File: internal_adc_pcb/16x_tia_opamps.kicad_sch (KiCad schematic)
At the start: 46 parts, among them U14 TLV9064, U15 TLV9064, U16 TLV9064, U17 TLV9064

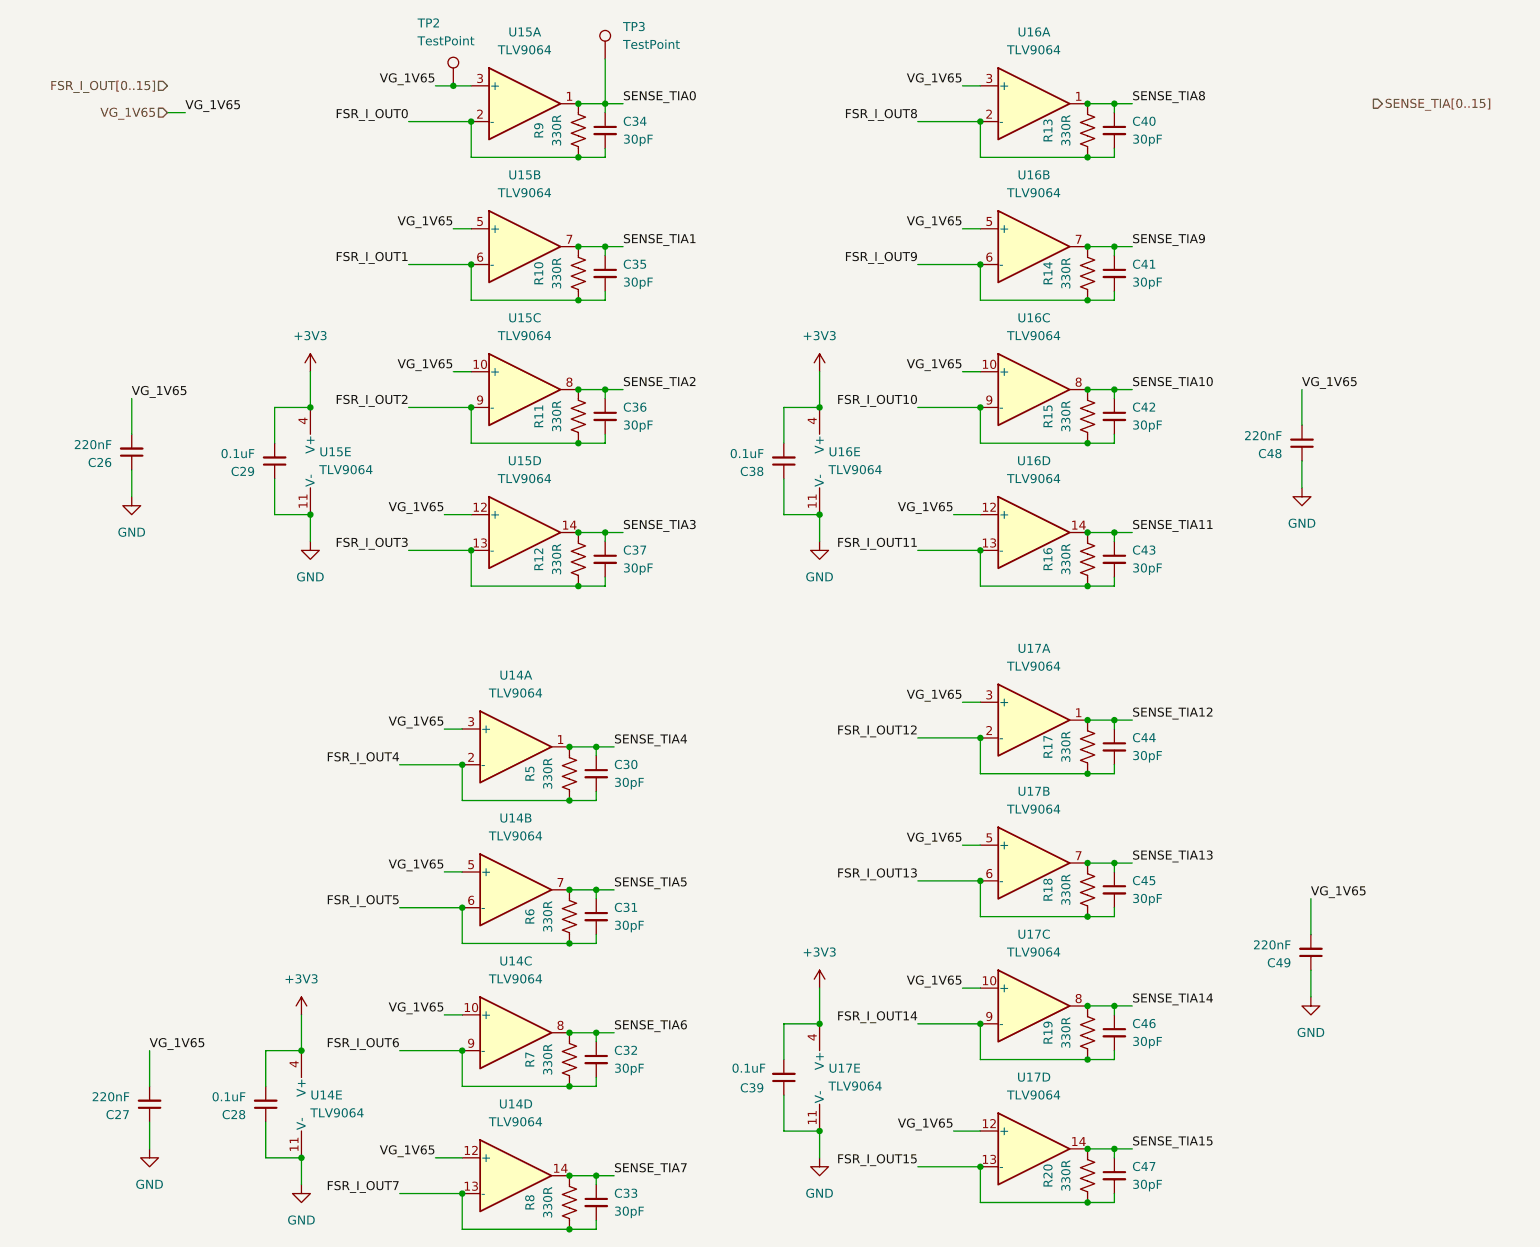
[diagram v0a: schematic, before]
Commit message: adjust VG issue for internal ADC version; changed naming for VG
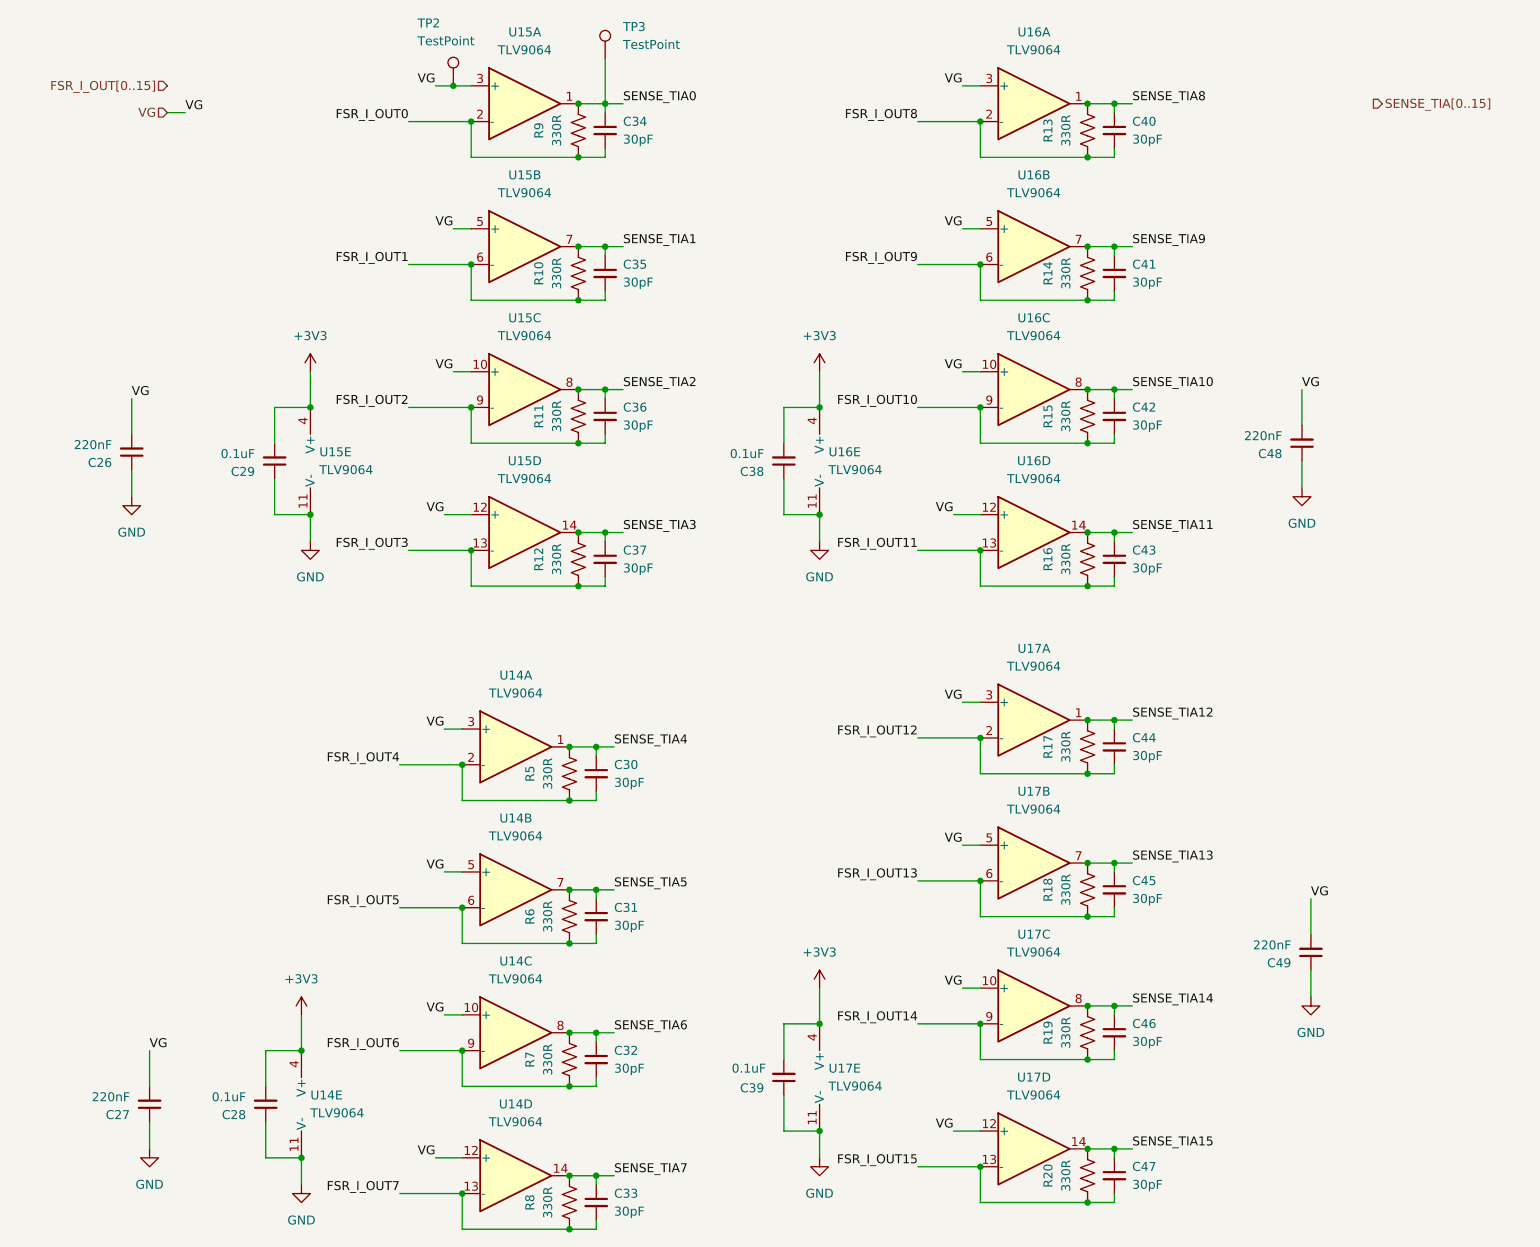
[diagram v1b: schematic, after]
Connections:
- net VG_1V65 renamed VG
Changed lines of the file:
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@@
 		)
 	)
-	(label "VG_1V65"
+	(label "VG"
 		(at 38.1 33.02 0)
 		(effects
@@
 		)
 	)
-	(label "VG_1V65"
+	(label "VG"
 		(at 76.2 69.85 180)
 		(effects
@@
 		)
 	)
-	(label "VG_1V65"
+	(label "VG"
 		(at 148.59 29.21 180)
 		(effects
@@
 		)
 	)
-	(label "VG_1V65"
+	(label "VG"
 		(at 148.59 49.53 180)
 		(effects
@@
 		)
 	)
-	(label "VG_1V65"
+	(label "VG"
 		(at 76.2 49.53 180)
 		(effects
@@
 		)
 	)
-	(label "VG_1V65"
+	(label "VG"
 		(at 147.32 90.17 180)
 		(effects
@@
 		)
 	)
-	(label "VG_1V65"
+	(label "VG"
 		(at 74.93 90.17 180)
 		(effects
@@
 		)
 	)
-	(label "VG_1V65"
+	(label "VG"
 		(at 147.32 177.8 180)
 		(effects
@@
 		)
 	)
-	(label "VG_1V65"
+	(label "VG"
 		(at 148.59 116.84 180)
 		(effects
@@
 		)
 	)
-	(label "VG_1V65"
+	(label "VG"
 		(at 74.93 120.65 180)
 		(effects
@@
 		)
 	)
-	(label "VG_1V65"
+	(label "VG"
 		(at 73.66 181.61 180)
 		(effects
@@
 		)
 	)
-	(label "VG_1V65"
+	(label "VG"
 		(at 196.85 72.39 0)
 		(effects
@@
 		)
 	)
-	(label "VG_1V65"
+	(label "VG"
 		(at 74.93 140.97 180)
 		(effects
@@
 		)
 	)
-	(label "VG_1V65"
+	(label "VG"
 		(at 30.48 73.66 0)
 		(effects
@@
 		)
 	)
-	(label "VG_1V65"
+	(label "VG"
 		(at 198.12 144.78 0)
 		(effects
@@
 		)
 	)
-	(label "VG_1V65"
+	(label "VG"
 		(at 148.59 137.16 180)
 		(effects
@@
 		)
 	)
-	(label "VG_1V65"
+	(label "VG"
 		(at 148.59 157.48 180)
 		(effects
@@
 		)
 	)
-	(label "VG_1V65"
+	(label "VG"
 		(at 73.66 29.21 180)
 		(effects
@@
 		)
 	)
-	(label "VG_1V65"
+	(label "VG"
 		(at 74.93 161.29 180)
 		(effects
@@
 		)
 	)
-	(label "VG_1V65"
+	(label "VG"
 		(at 148.59 69.85 180)
 		(effects
@@
 		)
 	)
-	(label "VG_1V65"
+	(label "VG"
 		(at 33.02 166.37 0)
 		(effects
@@
 		)
 	)
-	(hierarchical_label "VG_1V65"
+	(hierarchical_label "VG"
 		(shape input)
 		(at 35.56 33.02 180)

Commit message: update pcb for internal adc version
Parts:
- C26, C27, C28, C29, C30, C31, C32, C33, C34, C35, C36, C37, C38, C39, C40, C41, C42, C43, C44, C45, C46, C47, C48, C49, R10, R11, R12, R13, R14, R15, R16, R17, R18, R19, R20, R5, R6, R7, R8, R9: footprint (none) -> Capacitor_SMD:C_0603_1608Metric
- TP2, TP3: footprint (none) -> TestPoint:TestPoint_Keystone_5000-5004_Miniature
- U14, U15, U16, U17: footprint (none) -> Package_SO:TSSOP-14_4.4x5mm_P0.65mm
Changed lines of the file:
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@@
 			)
 		)
-		(property "Footprint" ""
+		(property "Footprint" "Capacitor_SMD:C_0603_1608Metric"
 			(at 30.48 81.28 0)
 			(hide yes)
@@
 			)
 		)
-		(property "Footprint" ""
+		(property "Footprint" "TestPoint:TestPoint_Keystone_5000-5004_Miniature"
 			(at 81.28 29.21 0)
 			(hide yes)
@@
 			)
 		)
-		(property "Footprint" ""
+		(property "Footprint" "Capacitor_SMD:C_0603_1608Metric"
 			(at 97.79 55.88 0)
 			(hide yes)
@@
 			)
 		)
-		(property "Footprint" ""
+		(property "Footprint" "Capacitor_SMD:C_0603_1608Metric"
 			(at 50.8 82.55 0)
 			(hide yes)
@@
 			)
 		)
-		(property "Footprint" ""
+		(property "Footprint" "Package_SO:TSSOP-14_4.4x5mm_P0.65mm"
 			(at 129.54 167.64 0)
 			(hide yes)
@@
 			)
 		)
-		(property "Footprint" ""
+		(property "Footprint" "Capacitor_SMD:C_0603_1608Metric"
 			(at 167.386 76.454 90)
 			(hide yes)
@@
 			)
 		)
-		(property "Footprint" ""
+		(property "Footprint" "Capacitor_SMD:C_0603_1608Metric"
 			(at 93.726 127.254 90)
 			(hide yes)
@@
 			)
 		)
-		(property "Footprint" ""
+		(property "Footprint" "Capacitor_SMD:C_0603_1608Metric"
 			(at 170.18 143.51 0)
 			(hide yes)
@@
 			)
 		)
-		(property "Footprint" ""
+		(property "Footprint" "Capacitor_SMD:C_0603_1608Metric"
 			(at 96.52 187.96 0)
 			(hide yes)
@@
 			)
 		)
-		(property "Footprint" ""
+		(property "Footprint" "Capacitor_SMD:C_0603_1608Metric"
 			(at 33.02 173.99 0)
 			(hide yes)
@@
 			)
 		)
-		(property "Footprint" ""
+		(property "Footprint" "Capacitor_SMD:C_0603_1608Metric"
 			(at 170.18 35.56 0)
 			(hide yes)
@@
 			)
 		)
-		(property "Footprint" ""
+		(property "Footprint" "Package_SO:TSSOP-14_4.4x5mm_P0.65mm"
 			(at 83.82 161.29 0)
 			(hide yes)
@@
 			)
 		)
-		(property "Footprint" ""
+		(property "Footprint" "Capacitor_SMD:C_0603_1608Metric"
 			(at 170.18 55.88 0)
 			(hide yes)
@@
 			)
 		)
-		(property "Footprint" ""
+		(property "Footprint" "Capacitor_SMD:C_0603_1608Metric"
 			(at 167.386 184.404 90)
 			(hide yes)
@@
 			)
 		)
-		(property "Footprint" ""
+		(property "Footprint" "Package_SO:TSSOP-14_4.4x5mm_P0.65mm"
 			(at 157.48 90.17 0)
 			(hide yes)
@@
 			)
 		)
-		(property "Footprint" ""
+		(property "Footprint" "Capacitor_SMD:C_0603_1608Metric"
 			(at 198.12 152.4 0)
 			(hide yes)
@@
 			)
 		)
-		(property "Footprint" ""
+		(property "Footprint" "Capacitor_SMD:C_0603_1608Metric"
 			(at 96.52 127 0)
 			(hide yes)
@@
 			)
 		)
-		(property "Footprint" ""
+		(property "Footprint" "Capacitor_SMD:C_0603_1608Metric"
 			(at 97.79 35.56 0)
 			(hide yes)
@@
 			)
 		)
-		(property "Footprint" ""
+		(property "Footprint" "Capacitor_SMD:C_0603_1608Metric"
 			(at 167.386 143.764 90)
 			(hide yes)
@@
 			)
 		)
-		(property "Footprint" ""
+		(property "Footprint" "Capacitor_SMD:C_0603_1608Metric"
 			(at 167.386 164.084 90)
 			(hide yes)
@@
 			)
 		)
-		(property "Footprint" ""
+		(property "Footprint" "Capacitor_SMD:C_0603_1608Metric"
 			(at 167.386 123.444 90)
 			(hide yes)
@@
 			)
 		)
-		(property "Footprint" ""
+		(property "Footprint" "Capacitor_SMD:C_0603_1608Metric"
 			(at 94.996 56.134 90)
 			(hide yes)
@@
 			)
 		)
-		(property "Footprint" ""
+		(property "Footprint" "Package_SO:TSSOP-14_4.4x5mm_P0.65mm"
 			(at 85.09 29.21 0)
 			(hide yes)
@@
 			)
 		)
-		(property "Footprint" ""
+		(property "Footprint" "Capacitor_SMD:C_0603_1608Metric"
 			(at 94.996 35.814 90)
 			(hide yes)
@@
 			)
 		)
-		(property "Footprint" ""
+		(property "Footprint" "Capacitor_SMD:C_0603_1608Metric"
 			(at 123.19 82.55 0)
 			(hide yes)
@@
 			)
 		)
-		(property "Footprint" ""
+		(property "Footprint" "Capacitor_SMD:C_0603_1608Metric"
 			(at 167.386 56.134 90)
 			(hide yes)
@@
 			)
 		)
-		(property "Footprint" ""
+		(property "Footprint" "Capacitor_SMD:C_0603_1608Metric"
 			(at 123.19 170.18 0)
 			(hide yes)
@@
 			)
 		)
-		(property "Footprint" ""
+		(property "Footprint" "Package_SO:TSSOP-14_4.4x5mm_P0.65mm"
 			(at 157.48 157.48 0)
 			(hide yes)
@@
 			)
 		)
-		(property "Footprint" ""
+		(property "Footprint" "Capacitor_SMD:C_0603_1608Metric"
 			(at 97.79 96.52 0)
 			(hide yes)
@@
 			)
 		)
-		(property "Footprint" ""
+		(property "Footprint" "Capacitor_SMD:C_0603_1608Metric"
 			(at 96.52 147.32 0)
 			(hide yes)
@@
 			)
 		)
-		(property "Footprint" ""
+		(property "Footprint" "Package_SO:TSSOP-14_4.4x5mm_P0.65mm"
 			(at 55.88 171.45 0)
 			(hide yes)
@@
 			)
 		)
-		(property "Footprint" ""
+		(property "Footprint" "Package_SO:TSSOP-14_4.4x5mm_P0.65mm"
 			(at 57.15 80.01 0)
 			(hide yes)
@@
 			)
 		)
-		(property "Footprint" ""
+		(property "Footprint" "Capacitor_SMD:C_0603_1608Metric"
 			(at 94.996 96.774 90)
 			(hide yes)
@@
 			)
 		)
-		(property "Footprint" ""
+		(property "Footprint" "Capacitor_SMD:C_0603_1608Metric"
 			(at 167.386 35.814 90)
 			(hide yes)
@@
 			)
 		)
-		(property "Footprint" ""
+		(property "Footprint" "Capacitor_SMD:C_0603_1608Metric"
 			(at 97.79 76.2 0)
 			(hide yes)
@@
 			)
 		)
-		(property "Footprint" ""
+		(property "Footprint" "Package_SO:TSSOP-14_4.4x5mm_P0.65mm"
 			(at 85.09 90.17 0)
 			(hide yes)
@@
 			)
 		)
-		(property "Footprint" ""
+		(property "Footprint" "Package_SO:TSSOP-14_4.4x5mm_P0.65mm"
 			(at 157.48 137.16 0)
 			(hide yes)
@@
 			)
 		)
-		(property "Footprint" ""
+		(property "Footprint" "Capacitor_SMD:C_0603_1608Metric"
 			(at 170.18 163.83 0)
 			(hide yes)
@@
 			)
 		)
-		(property "Footprint" ""
+		(property "Footprint" "Capacitor_SMD:C_0603_1608Metric"
 			(at 93.726 188.214 90)
 			(hide yes)
@@
 			)
 		)
-		(property "Footprint" ""
+		(property "Footprint" "Capacitor_SMD:C_0603_1608Metric"
 			(at 196.85 80.01 0)
 			(hide yes)
@@
 			)
 		)
-		(property "Footprint" ""
+		(property "Footprint" "Capacitor_SMD:C_0603_1608Metric"
 			(at 170.18 123.19 0)
 			(hide yes)
@@
 			)
 		)
-		(property "Footprint" ""
+		(property "Footprint" "Capacitor_SMD:C_0603_1608Metric"
 			(at 170.18 184.15 0)
 			(hide yes)
@@
 			)
 		)
-		(property "Footprint" ""
+		(property "Footprint" "Package_SO:TSSOP-14_4.4x5mm_P0.65mm"
 			(at 157.48 49.53 0)
 			(hide yes)
@@
 			)
 		)
-		(property "Footprint" ""
+		(property "Footprint" "Package_SO:TSSOP-14_4.4x5mm_P0.65mm"
 			(at 157.48 116.84 0)
 			(hide yes)
@@
 			)
 		)
-		(property "Footprint" ""
+		(property "Footprint" "Capacitor_SMD:C_0603_1608Metric"
 			(at 49.53 173.99 0)
 			(hide yes)
@@
 			)
 		)
-		(property "Footprint" ""
+		(property "Footprint" "Package_SO:TSSOP-14_4.4x5mm_P0.65mm"
 			(at 157.48 29.21 0)
 			(hide yes)
@@
 			)
 		)
-		(property "Footprint" ""
+		(property "Footprint" "Package_SO:TSSOP-14_4.4x5mm_P0.65mm"
 			(at 85.09 69.85 0)
 			(hide yes)
@@
 			)
 		)
-		(property "Footprint" ""
+		(property "Footprint" "Capacitor_SMD:C_0603_1608Metric"
 			(at 93.726 167.894 90)
 			(hide yes)
@@
 			)
 		)
-		(property "Footprint" ""
+		(property "Footprint" "Package_SO:TSSOP-14_4.4x5mm_P0.65mm"
 			(at 83.82 181.61 0)
 			(hide yes)
@@
 			)
 		)
-		(property "Footprint" ""
+		(property "Footprint" "Capacitor_SMD:C_0603_1608Metric"
 			(at 167.386 96.774 90)
 			(hide yes)
@@
 			)
 		)
-		(property "Footprint" ""
+		(property "Footprint" "TestPoint:TestPoint_Keystone_5000-5004_Miniature"
 			(at 102.87 25.4 0)
 			(hide yes)
@@
 			)
 		)
-		(property "Footprint" ""
+		(property "Footprint" "Package_SO:TSSOP-14_4.4x5mm_P0.65mm"
 			(at 83.82 140.97 0)
 			(hide yes)
@@
 			)
 		)
-		(property "Footprint" ""
+		(property "Footprint" "Capacitor_SMD:C_0603_1608Metric"
 			(at 96.52 167.64 0)
 			(hide yes)
@@
 			)
 		)
-		(property "Footprint" ""
+		(property "Footprint" "Package_SO:TSSOP-14_4.4x5mm_P0.65mm"
 			(at 157.48 69.85 0)
 			(hide yes)
@@
 			)
 		)
-		(property "Footprint" ""
+		(property "Footprint" "Capacitor_SMD:C_0603_1608Metric"
 			(at 94.996 76.454 90)
 			(hide yes)
@@
 			)
 		)
-		(property "Footprint" ""
+		(property "Footprint" "Package_SO:TSSOP-14_4.4x5mm_P0.65mm"
 			(at 157.48 177.8 0)
 			(hide yes)
@@
 			)
 		)
-		(property "Footprint" ""
+		(property "Footprint" "Capacitor_SMD:C_0603_1608Metric"
 			(at 93.726 147.574 90)
 			(hide yes)
@@
 			)
 		)
-		(property "Footprint" ""
+		(property "Footprint" "Package_SO:TSSOP-14_4.4x5mm_P0.65mm"
 			(at 83.82 120.65 0)
 			(hide yes)
@@
 			)
 		)
-		(property "Footprint" ""
+		(property "Footprint" "Package_SO:TSSOP-14_4.4x5mm_P0.65mm"
 			(at 85.09 49.53 0)
 			(hide yes)
@@
 			)
 		)
-		(property "Footprint" ""
+		(property "Footprint" "Capacitor_SMD:C_0603_1608Metric"
 			(at 170.18 76.2 0)
 			(hide yes)
@@
 			)
 		)
-		(property "Footprint" ""
+		(property "Footprint" "Package_SO:TSSOP-14_4.4x5mm_P0.65mm"
 			(at 129.54 80.01 0)
 			(hide yes)
@@
 			)
 		)
-		(property "Footprint" ""
+		(property "Footprint" "Capacitor_SMD:C_0603_1608Metric"
 			(at 170.18 96.52 0)
 			(hide yes)

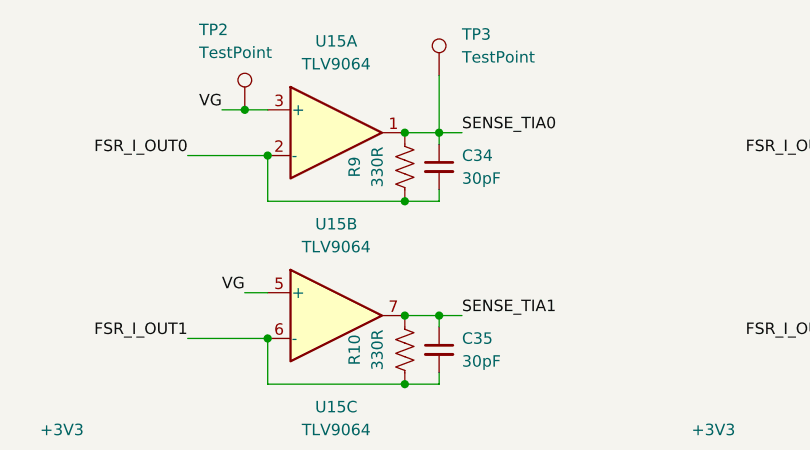
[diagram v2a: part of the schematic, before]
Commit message: done all 4 TIA opamps for internal adc version
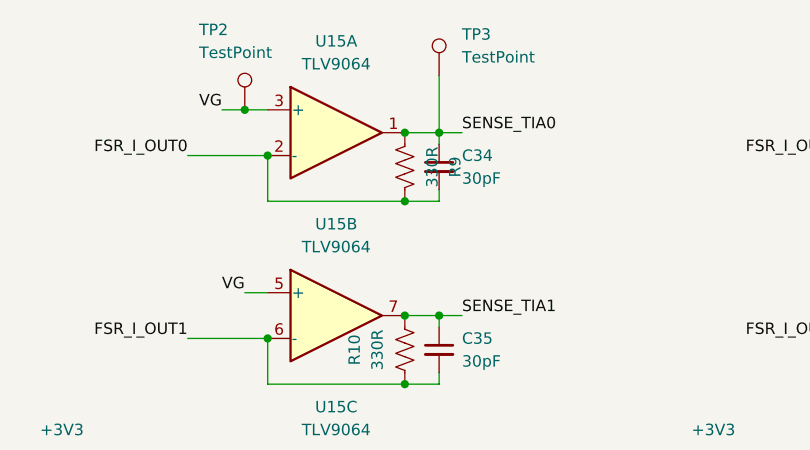
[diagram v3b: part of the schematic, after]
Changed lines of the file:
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@@
 		(lib_id "Device:R_US")
 		(at 93.98 35.56 0)
+		(mirror y)
 		(unit 1)
 		(body_style 1)
@@
 		(dnp no)
 		(property "Reference" "R9"
-			(at 88.392 35.56 90)
+			(at 99.568 35.56 90)
 			(show_name no)
 			(do_not_autoplace no)
@@
 		)
 		(property "Value" "330R"
-			(at 90.932 35.56 90)
+			(at 97.028 35.56 90)
 			(show_name no)
 			(do_not_autoplace no)
@@
 		)
 		(property "Footprint" "Capacitor_SMD:C_0603_1608Metric"
-			(at 94.996 35.814 90)
+			(at 92.964 35.814 90)
 			(hide yes)
 			(show_name no)
